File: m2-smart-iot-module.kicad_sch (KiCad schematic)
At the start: 3 parts

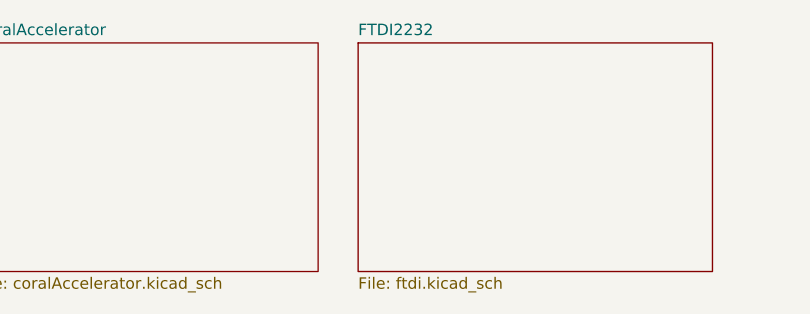
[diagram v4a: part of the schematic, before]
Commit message: Replaced ft2232 with ft4232H
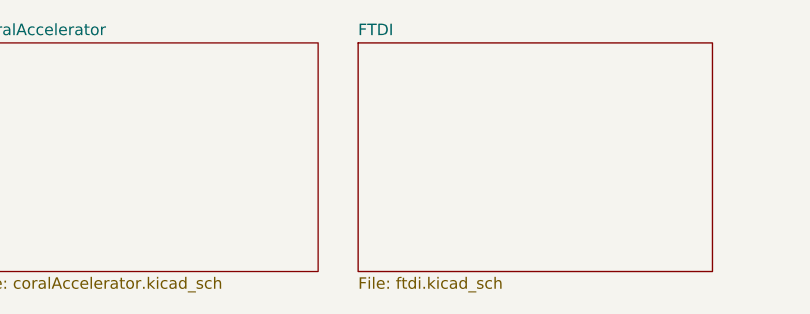
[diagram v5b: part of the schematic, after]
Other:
- sheet FTDI2232 renamed FTDI
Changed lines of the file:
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@@
     (stroke (width 0.1524) (type solid) (color 0 0 0 0))
     (fill (color 0 0 0 0.0000))
-    (property "Sheet name" "FTDI2232" (id 0) (at 295.275 113.5884 0)
+    (property "Sheet name" "FTDI" (id 0) (at 295.275 113.5884 0)
       (effects (font (size 1.27 1.27)) (justify left bottom))
     )
@@
     )
     (path "/68410b93-aca6-44d3-bd1e-cd427080a29c/3f5a84f7-9e18-4808-aab2-0e69509107a0"
-      (reference "U1") (unit 1) (value "FT2232H-56Q") (footprint "antmicro-footprints:QFN-56-1EP_8x8mm_P0.5mm_EP5.5.9x5.9mm")
+      (reference "U1") (unit 1) (value "FT4232H-56Q") (footprint "antmicro-footprints:QFN-56-1EP_8x8mm_P0.5mm_EP5.5.9x5.9mm")
     )
     (path "/00000000-0000-0000-0000-0000604cff57/00000000-0000-0000-0000-0000604de031"
